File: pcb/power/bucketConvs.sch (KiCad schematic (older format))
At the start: 20 parts, among them U1 LM2840, U2 TS30012

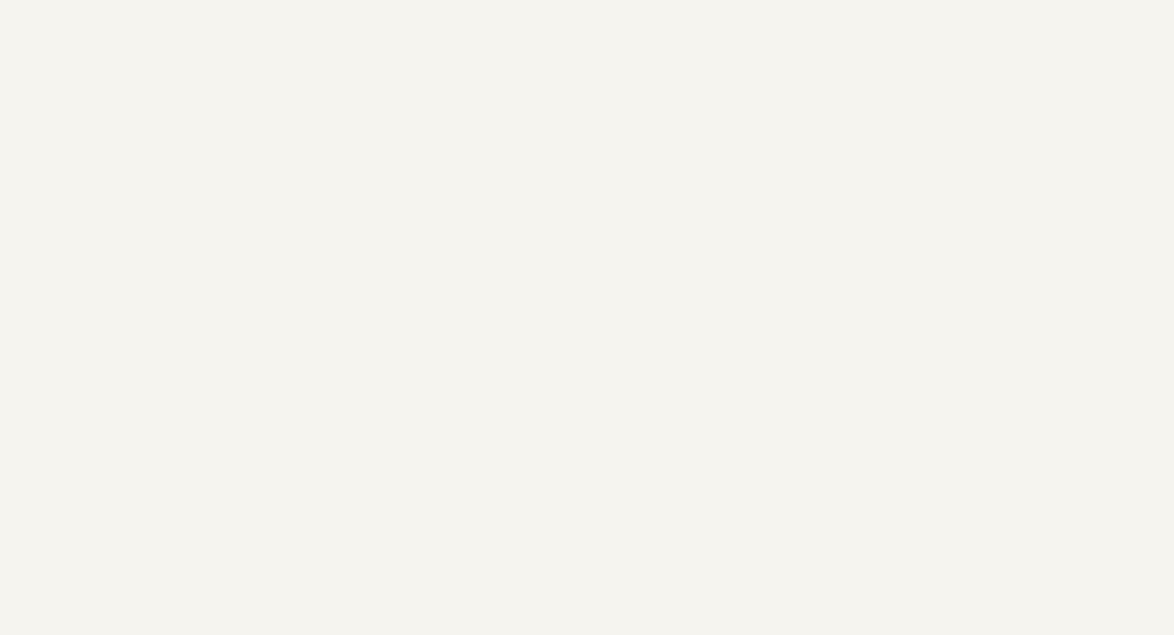
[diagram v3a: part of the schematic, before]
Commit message: Started completely over with the layout, as the OLED would not fit anymore. Also introduced a USB DCP Controller and found a stupid bug in the LED driver.
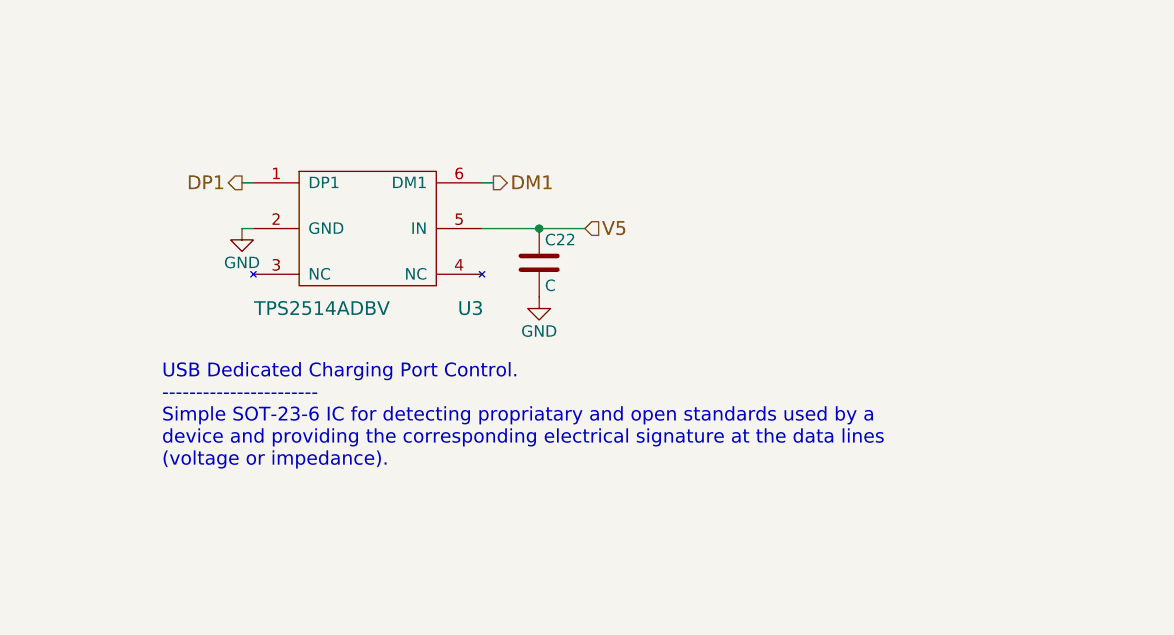
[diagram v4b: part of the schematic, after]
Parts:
- added C22: C, Capacitors_SMD:C_0603_HandSoldering, symbol C
- added U3: TPS2514ADBV, TO_SOT_Packages_SMD:SOT-23-6, symbol TPS2514ADBV
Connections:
- net GND: now also C22.2, U3.2 (GND)
- net V5: now also C22.1, U3.5 (IN)
- new net DM1: U3.6 (DM1)
- new net DP1: U3.1 (DP1)
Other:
- note added: "USB Dedicated Charging Port Control.\n-----------------------\nSimple SOT-23-6 IC for detecting propriatary and open standards used by a\ndevice and providing the corresponding electrical signature at the data lines\n(voltage or impedance)."
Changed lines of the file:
@@
 Sheet 2 5
 Title "Bucket Converters for 5 V and 2.8 V"
-Date "2016-12-02"
+Date "2016-12-29"
 Rev "1.0"
 Comp "Uppsala University"
@@
 $EndComp
 $Comp
-L GND #PWR07
+L GND #PWR5
 U 1 1 5842EC4A
 P 1700 2550
-F 0 "#PWR07" H 1700 2300 50  0001 C CNN
+F 0 "#PWR5" H 1700 2300 50  0001 C CNN
 F 1 "GND" H 1700 2400 50  0000 C CNN
 F 2 "" H 1700 2550 50  0000 C CNN
@@
 $EndComp
 $Comp
-L GND #PWR08
+L GND #PWR7
 U 1 1 5842EC58
 P 3000 3600
-F 0 "#PWR08" H 3000 3350 50  0001 C CNN
+F 0 "#PWR7" H 3000 3350 50  0001 C CNN
 F 1 "GND" H 3000 3450 50  0000 C CNN
 F 2 "" H 3000 3600 50  0000 C CNN
@@
 $EndComp
 $Comp
-L GND #PWR09
+L GND #PWR6
 U 1 1 5842F8AB
 P 1800 5650
-F 0 "#PWR09" H 1800 5400 50  0001 C CNN
+F 0 "#PWR6" H 1800 5400 50  0001 C CNN
 F 1 "GND" H 1800 5500 50  0000 C CNN
 F 2 "" H 1800 5650 50  0000 C CNN
@@
 5V for Mobile Phone\n-----------------------\nVout,max=5 V\nAout,max = 2A
 $Comp
-L GND #PWR010
+L GND #PWR8
 U 1 1 5842F92D
 P 3100 6050
-F 0 "#PWR010" H 3100 5800 50  0001 C CNN
+F 0 "#PWR8" H 3100 5800 50  0001 C CNN
 F 1 "GND" H 3100 5900 50  0000 C CNN
 F 2 "" H 3100 6050 50  0000 C CNN
@@
 $EndComp
 $Comp
-L GND #PWR011
+L GND #PWR9
 U 1 1 5842F939
 P 4100 5200
-F 0 "#PWR011" H 4100 4950 50  0001 C CNN
+F 0 "#PWR9" H 4100 4950 50  0001 C CNN
 F 1 "GND" H 4100 5050 50  0000 C CNN
 F 2 "" H 4100 5200 50  0000 C CNN
@@
 $EndComp
 $Comp
-L PWR_FLAG #FLG012
+L PWR_FLAG #FLG3
 U 1 1 5842F941
 P 5750 5250
-F 0 "#FLG012" H 5750 5345 50  0001 C CNN
+F 0 "#FLG3" H 5750 5345 50  0001 C CNN
 F 1 "PWR_FLAG" H 5750 5430 50  0000 C CNN
 F 2 "" H 5750 5250 50  0000 C CNN
@@
 Connection ~ 4800 2400
 $Comp
-L GND #PWR013
+L GND #PWR10
 U 1 1 584C8E69
 P 6600 6350
-F 0 "#PWR013" H 6600 6100 50  0001 C CNN
+F 0 "#PWR10" H 6600 6100 50  0001 C CNN
 F 1 "GND" H 6600 6200 50  0000 C CNN
 F 2 "" H 6600 6350 50  0000 C CNN
@@
 $EndComp
 Connection ~ 6600 6300
+$Comp
+L TPS2514ADBV U3
+U 1 1 5865A2F4
+P 7900 3500
+F 0 "U3" H 8350 3150 60  0000 C CNN
+F 1 "TPS2514ADBV" H 7700 3150 60  0000 C CNN
+F 2 "TO_SOT_Packages_SMD:SOT-23-6" H 7900 3500 60  0001 C CNN
+F 3 "http://www.ti.com/lit/ds/symlink/tps2514a.pdf" H 7900 3500 60  0001 C CNN
+F 4 "296-40725-1-ND" H 7900 3500 60  0001 C CNN "Digikey"
+	1    7900 3500
+	1    0    0    -1
+$EndComp
+Text HLabel 8850 3500 2    60   Input ~ 0
+V5
+$Comp
+L GND #PWR11
+U 1 1 5865A9E7
+P 7350 3500
+F 0 "#PWR11" H 7350 3250 50  0001 C CNN
+F 1 "GND" H 7350 3350 50  0000 C CNN
+F 2 "" H 7350 3500 50  0000 C CNN
+F 3 "" H 7350 3500 50  0000 C CNN
+	1    7350 3500
+	1    0    0    -1
+$EndComp
+Wire Wire Line
+	7350 3500 7400 3500
+Text Notes 7000 4550 0    60   ~ 0
+USB Dedicated Charging Port Control.\n-----------------------\nSimple SOT-23-6 IC for detecting propriatary and open standards used by a\ndevice and providing the corresponding electrical signature at the data lines\n(voltage or impedance).
+Text HLabel 8450 3300 2    60   Output ~ 0
+DM1
+Wire Wire Line
+	8400 3300 8450 3300
+Text HLabel 7350 3300 0    60   Output ~ 0
+DP1
+Wire Wire Line
+	7400 3300 7350 3300
+$Comp
+L C C22
+U 1 1 586629FF
+P 8650 3650
+F 0 "C22" H 8675 3750 50  0000 L CNN
+F 1 "C" H 8675 3550 50  0000 L CNN
+F 2 "Capacitors_SMD:C_0603_HandSoldering" H 8688 3500 50  0001 C CNN
+F 3 "http://www.yageo.com/documents/recent/UPY-GPHC_Y5V_6.3V-to-50V_6.pdf" H 8650 3650 50  0001 C CNN
+F 4 "311-1343-1-ND" H 8650 3650 60  0001 C CNN "Digikey"
+	1    8650 3650
+	1    0    0    -1
+$EndComp
+Wire Wire Line
+	8400 3500 8850 3500
+Connection ~ 8650 3500
+$Comp
+L GND #PWR12
+U 1 1 58662C1C
+P 8650 3800
+F 0 "#PWR12" H 8650 3550 50  0001 C CNN
+F 1 "GND" H 8650 3650 50  0000 C CNN
+F 2 "" H 8650 3800 50  0000 C CNN
+F 3 "" H 8650 3800 50  0000 C CNN
+	1    8650 3800
+	1    0    0    -1
+$EndComp
 $EndSCHEMATC

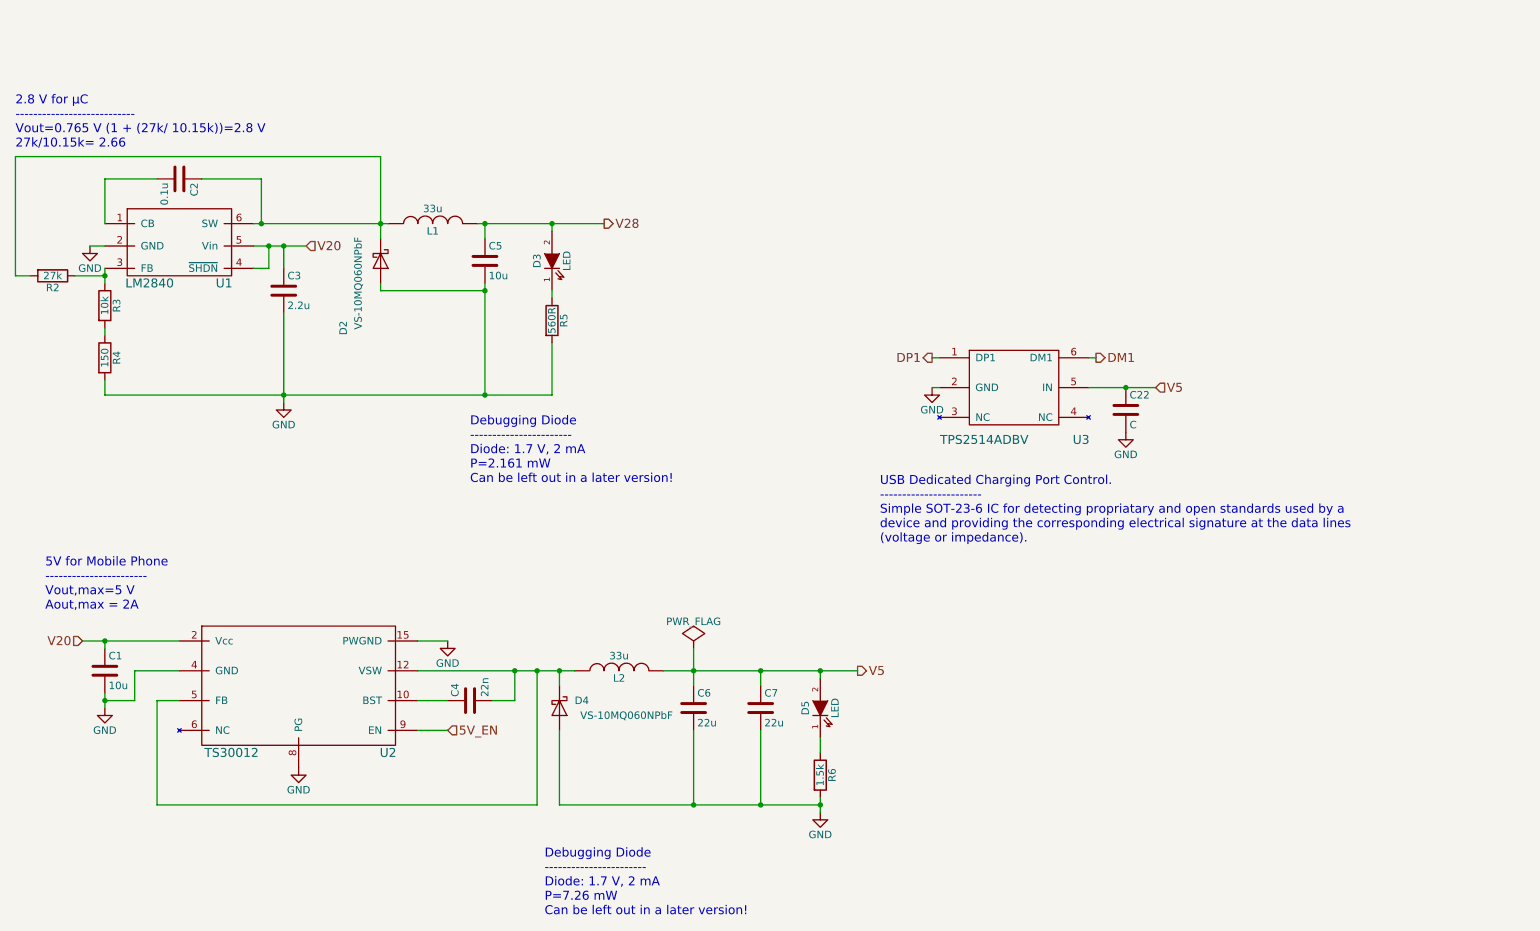
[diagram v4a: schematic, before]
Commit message: Fixed the bug. Now workin with differential amplifiers. Started over once more with the layout.
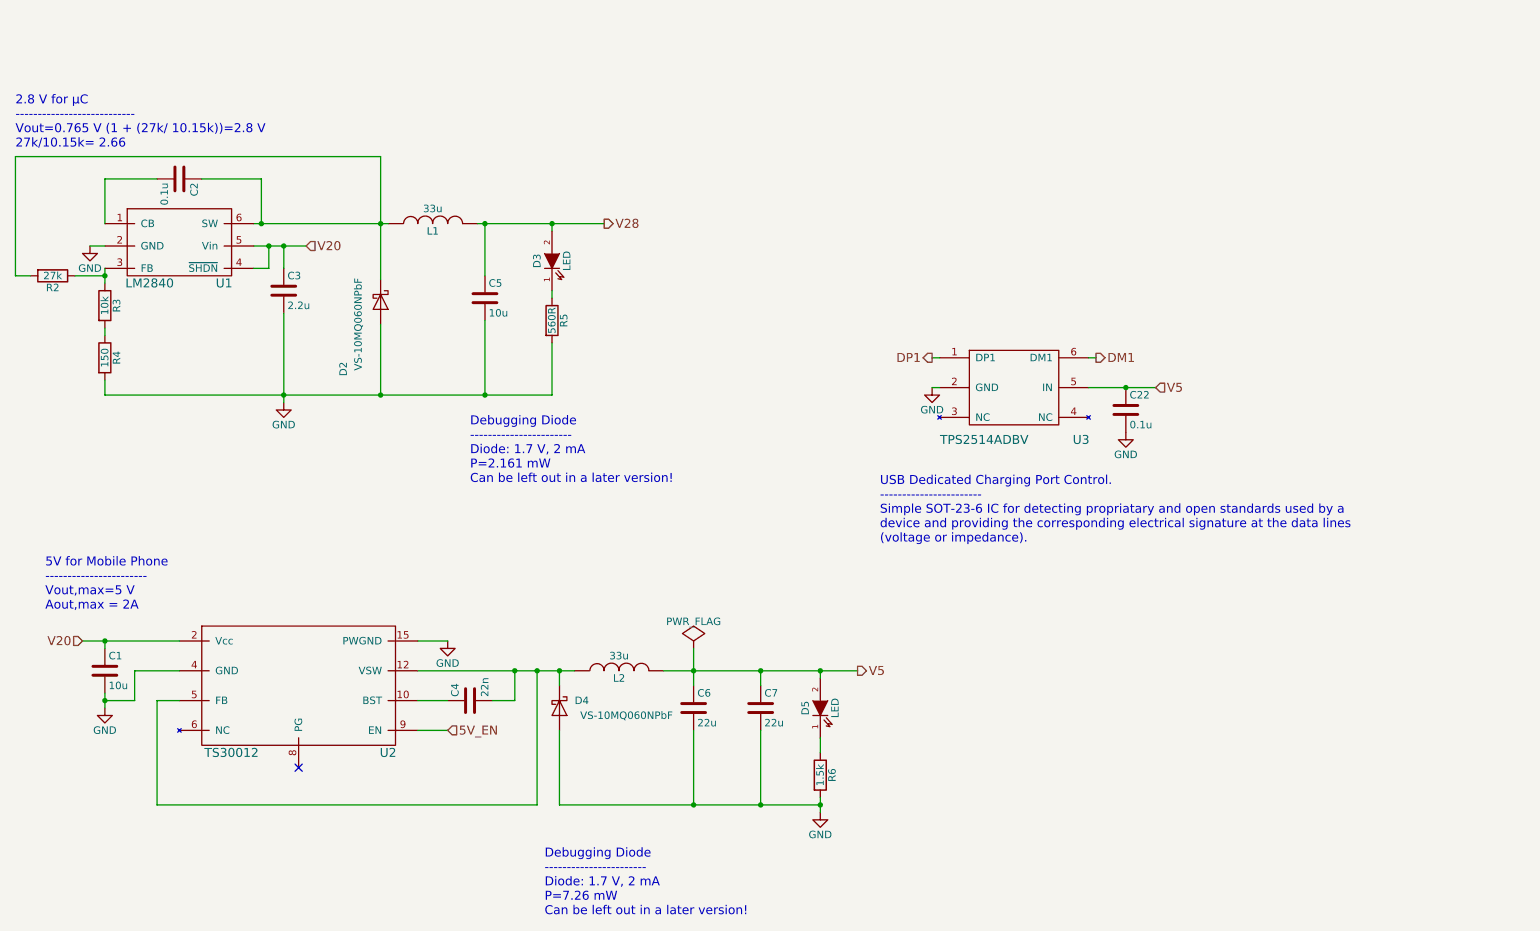
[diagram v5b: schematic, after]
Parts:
- C22: value C -> 0.1u
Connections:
- net GND: no longer U2.8 (PG)
- no-connect marks 0 -> 1
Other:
- moved on the sheet: C5, D2
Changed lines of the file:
@@
 Sheet 2 5
 Title "Bucket Converters for 5 V and 2.8 V"
-Date "2016-12-29"
+Date "2016-12-30"
 Rev "1.0"
 Comp "Uppsala University"
@@
 L C C5
 U 1 1 5842EC80
-P 4350 2650
-F 0 "C5" H 4375 2750 50  0000 L CNN
-F 1 "10u" H 4375 2550 50  0000 L CNN
-F 2 "Capacitors_SMD:C_0603_HandSoldering" H 4388 2500 50  0001 C CNN
-F 3 "http://search.murata.co.jp/Ceramy/image/img/A01X/G101/ENG/GRT188R61E106ME13-01.pdf" H 4350 2650 50  0001 C CNN
-F 4 "490-12323-1-ND" H 4350 2650 60  0001 C CNN "Digikey"
-	1    4350 2650
+P 4350 2900
+F 0 "C5" H 4375 3000 50  0000 L CNN
+F 1 "10u" H 4375 2800 50  0000 L CNN
+F 2 "Capacitors_SMD:C_0603_HandSoldering" H 4388 2750 50  0001 C CNN
+F 3 "http://search.murata.co.jp/Ceramy/image/img/A01X/G101/ENG/GRT188R61E106ME13-01.pdf" H 4350 2900 50  0001 C CNN
+F 4 "490-12323-1-ND" H 4350 2900 60  0001 C CNN "Digikey"
+	1    4350 2900
 	1    0    0    -1
 $EndComp
@@
 L D_Schottky D2
 U 1 1 5842ECC9
-P 3650 2650
-F 0 "D2" H 4100 2400 50  0000 C CNN
-F 1 "VS-10MQ060NPbF" H 3800 2500 50  0000 C CNN
-F 2 "Diodes_SMD:SMA_Handsoldering" H 3650 2650 50  0001 C CNN
-F 3 "http://www.vishay.com/docs/88869/packaging.pdf" H 3650 2650 50  0001 C CNN
-F 4 "10MQ060NPBFCT-ND" V 3700 3250 60  0001 C CNN "Digikey"
-	1    3650 2650
+P 3650 2925
+F 0 "D2" H 4100 2675 50  0000 C CNN
+F 1 "VS-10MQ060NPbF" H 3800 2775 50  0000 C CNN
+F 2 "Diodes_SMD:SMA_Handsoldering" H 3650 2925 50  0001 C CNN
+F 3 "http://www.vishay.com/docs/88869/packaging.pdf" H 3650 2925 50  0001 C CNN
+F 4 "10MQ060NPBFCT-ND" V 3700 3525 60  0001 C CNN "Digikey"
+	1    3650 2925
 	0    1    1    0
 $EndComp
@@
 $Comp
 L GND #PWR8
-U 1 1 5842F92D
-P 3100 6050
-F 0 "#PWR8" H 3100 5800 50  0001 C CNN
-F 1 "GND" H 3100 5900 50  0000 C CNN
-F 2 "" H 3100 6050 50  0000 C CNN
-F 3 "" H 3100 6050 50  0000 C CNN
-	1    3100 6050
-	1    0    0    -1
-$EndComp
-$Comp
-L GND #PWR9
 U 1 1 5842F939
 P 4100 5200
-F 0 "#PWR9" H 4100 4950 50  0001 C CNN
+F 0 "#PWR8" H 4100 4950 50  0001 C CNN
 F 1 "GND" H 4100 5050 50  0000 C CNN
 F 2 "" H 4100 5200 50  0000 C CNN
@@
 Connection ~ 2850 2400
 Wire Wire Line
-	3650 1950 3650 2500
+	3650 1950 3650 2775
 Connection ~ 3650 2400
 Wire Wire Line
-	4350 2400 4350 2500
-Wire Wire Line
-	4350 2850 3650 2850
-Wire Wire Line
-	3650 2850 3650 2800
+	4350 2400 4350 2750
+Wire Wire Line
+	3650 3550 3650 3075
 Connection ~ 4350 2400
 Wire Wire Line
@@
 	1200 2750 1300 2750
 Connection ~ 3000 3550
-Connection ~ 4350 2850
 Wire Wire Line
 	1800 3550 1800 3450
-Wire Wire Line
-	4350 3550 4350 2800
 Wire Wire Line
 	2800 2550 3150 2550
@@
 Connection ~ 4800 2400
 $Comp
-L GND #PWR10
+L GND #PWR9
 U 1 1 584C8E69
 P 6600 6350
-F 0 "#PWR10" H 6600 6100 50  0001 C CNN
+F 0 "#PWR9" H 6600 6100 50  0001 C CNN
 F 1 "GND" H 6600 6200 50  0000 C CNN
 F 2 "" H 6600 6350 50  0000 C CNN
@@
 V5
 $Comp
-L GND #PWR11
+L GND #PWR10
 U 1 1 5865A9E7
 P 7350 3500
-F 0 "#PWR11" H 7350 3250 50  0001 C CNN
+F 0 "#PWR10" H 7350 3250 50  0001 C CNN
 F 1 "GND" H 7350 3350 50  0000 C CNN
 F 2 "" H 7350 3500 50  0000 C CNN
@@
 P 8650 3650
 F 0 "C22" H 8675 3750 50  0000 L CNN
-F 1 "C" H 8675 3550 50  0000 L CNN
+F 1 "0.1u" H 8675 3550 50  0000 L CNN
 F 2 "Capacitors_SMD:C_0603_HandSoldering" H 8688 3500 50  0001 C CNN
 F 3 "http://www.yageo.com/documents/recent/UPY-GPHC_Y5V_6.3V-to-50V_6.pdf" H 8650 3650 50  0001 C CNN
@@
 Connection ~ 8650 3500
 $Comp
-L GND #PWR12
+L GND #PWR11
 U 1 1 58662C1C
 P 8650 3800
-F 0 "#PWR12" H 8650 3550 50  0001 C CNN
+F 0 "#PWR11" H 8650 3550 50  0001 C CNN
 F 1 "GND" H 8650 3650 50  0000 C CNN
 F 2 "" H 8650 3800 50  0000 C CNN
@@
 	1    0    0    -1
 $EndComp
+NoConn ~ 3100 6050
+Wire Wire Line
+	4350 3550 4350 3050
+Connection ~ 3650 3550
 $EndSCHEMATC
